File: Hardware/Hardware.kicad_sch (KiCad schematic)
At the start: 0 parts

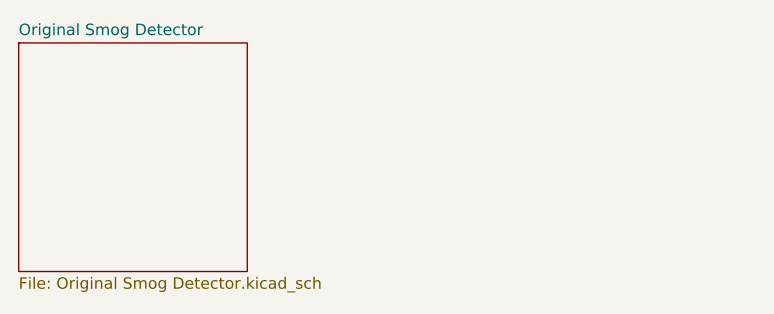
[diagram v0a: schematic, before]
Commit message: Made sheet Signal Amplification
will handle
- AC coupling of input
- DC biasing to 3V3/2
- Amplification by approx *-60
- Lowpass based anti-aliasing
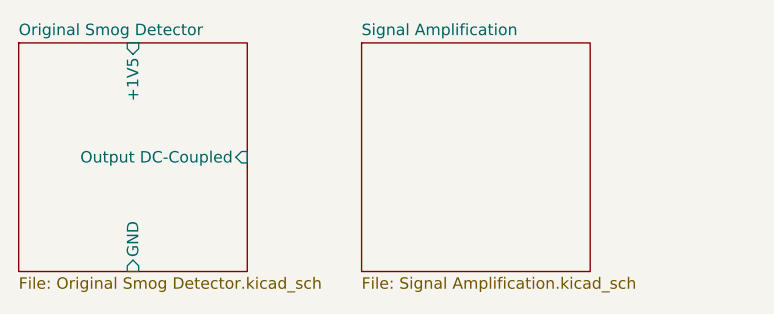
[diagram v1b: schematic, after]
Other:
- added sheet Signal Amplification (Signal Amplification.kicad_sch)
- sheet Original Smog Detector ports: added +1V5, GND, Output DC-Coupled; removed none
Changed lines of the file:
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@@
+			)
+		)
+		(pin "GND" input
+			(at 38.1 50.8 270)
+			(effects
+				(font
+					(size 1.27 1.27)
+				)
+				(justify left)
+			)
+		)
+		(pin "+1V5" input
+			(at 38.1 25.4 90)
+			(effects
+				(font
+					(size 1.27 1.27)
+				)
+				(justify right)
+			)
+		)
+		(pin "Output DC-Coupled" input
+			(at 50.8 38.1 0)
+			(effects
+				(font
+					(size 1.27 1.27)
+				)
+				(justify right)
 			)
 		)
@@
 				)
 			)
+		)
+	)
+	(sheet
+		(at 63.5 25.4)
+		(size 25.4 25.4)
+		(fields_autoplaced yes)
+		(stroke
+			(width 0.1524)
+			(type solid)
+		)
+		(fill
+			(color 0 0 0 0.0000)
+		)
+		(property "Sheetname" "Signal Amplification"
+			(at 63.5 24.6884 0)
+			(effects
+				(font
+					(size 1.27 1.27)
+				)
+				(justify left bottom)
+			)
+		)
+		(property "Sheetfile" "Signal Amplification.kicad_sch"
+			(at 63.5 51.3846 0)
+			(effects
+				(font
+					(size 1.27 1.27)
+				)
+				(justify left top)
+			)
+		)
+		(instances
+			(project "Hardware"
+				(path "/4e457c11-25d4-4677-9942-6ed7396aaf8a"
+					(page "3")
+				)
+			)

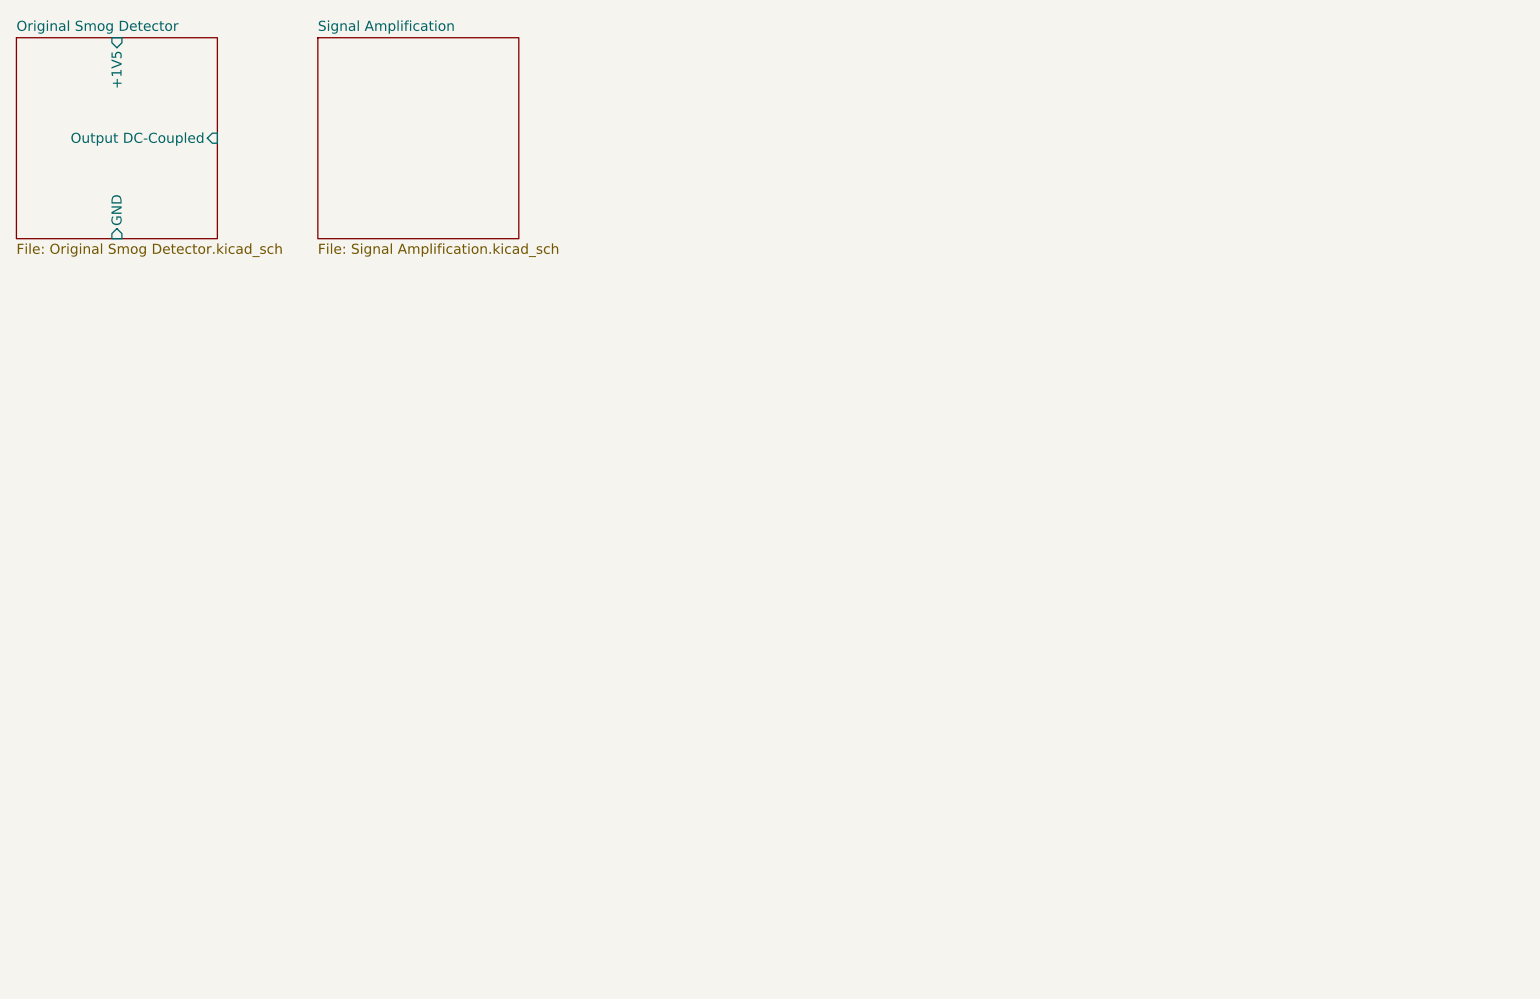
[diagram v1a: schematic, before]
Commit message: split some of the text and grouped the circuits better
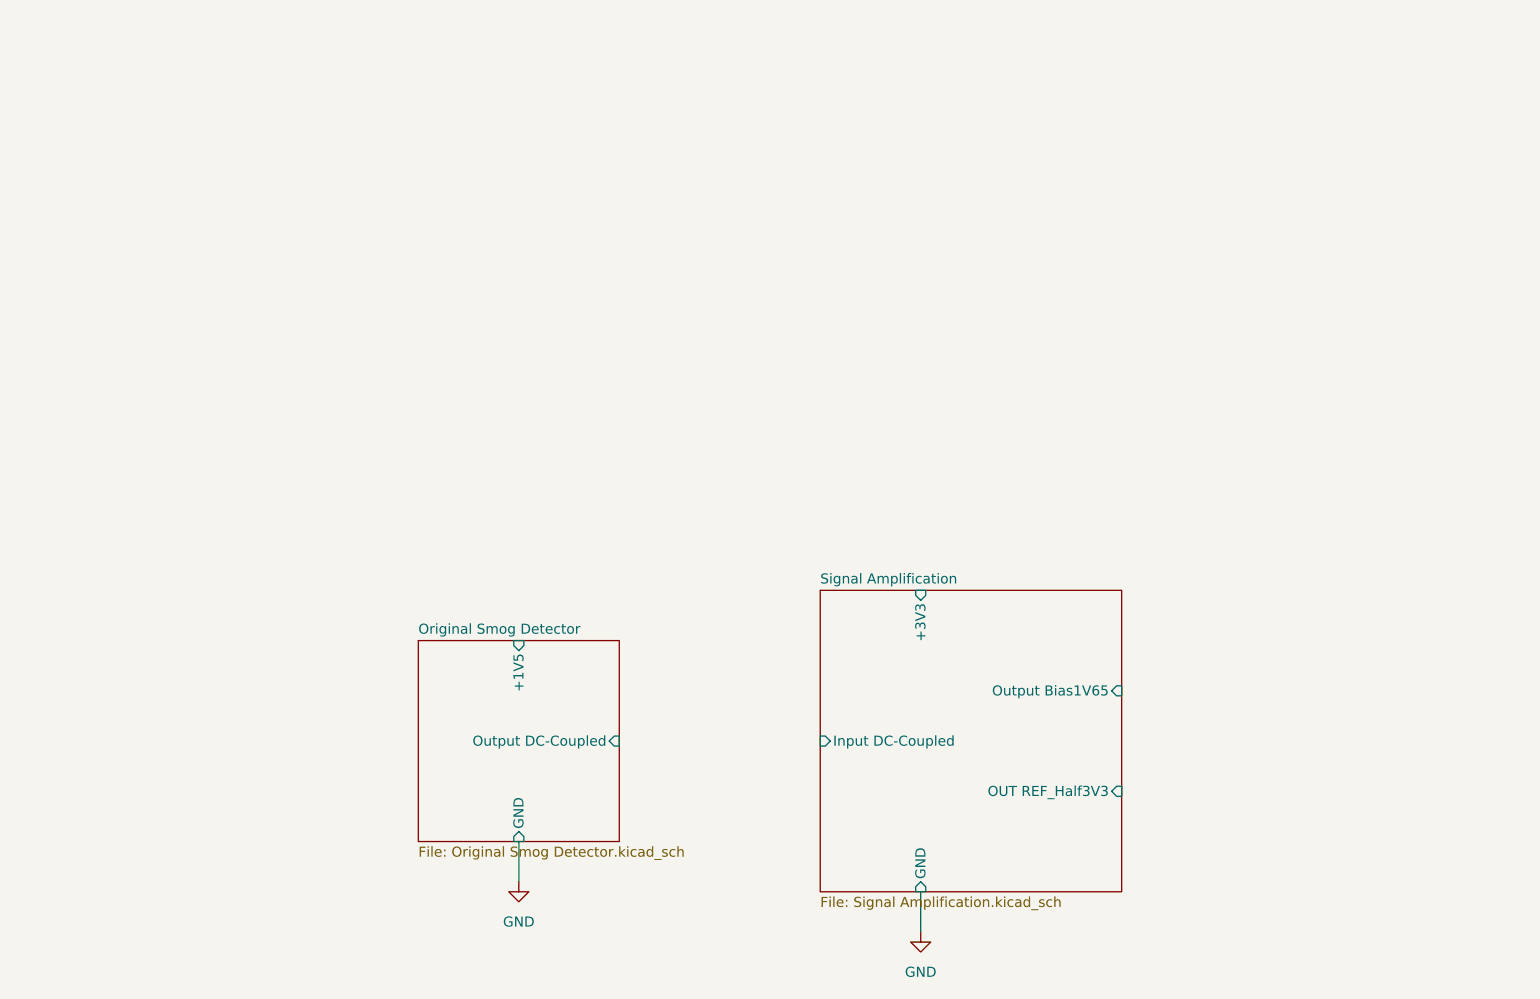
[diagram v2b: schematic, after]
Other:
- sheet Signal Amplification ports: added +3V3, GND, Input DC-Coupled, OUT REF_Half3V3, Output Bias1V65; removed none
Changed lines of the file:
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@@
 	(generator_version "8.0")
 	(paper "A4")
+	(wire
+		(pts
+			(xy 139.7 133.35) (xy 139.7 138.43)
+		)
+		(stroke
+			(width 0)
+			(type default)
+		)
+	)
+	(wire
+		(pts
+			(xy 88.9 127) (xy 88.9 132.08)
+		)
+		(stroke
+			(width 0)
+			(type default)
+		)
+	)
+	(symbol
+		(lib_id "power:GND")
+		(at 139.7 138.43 0)
+		(unit 1)
+		(exclude_from_sim no)
+		(in_bom yes)
+		(on_board yes)
+		(dnp no)
+		(fields_autoplaced yes)
+		(property "Reference" "#PWR02"
+			(at 139.7 144.78 0)
+			(effects
+				(font
+					(size 1.27 1.27)
+				)
+				(hide yes)
+			)
+		)
+		(property "Value" "GND"
+			(at 139.7 143.51 0)
+			(effects
+				(font
+					(size 1.27 1.27)
+				)
+			)
+		)
+		(property "Footprint" ""
+			(at 139.7 138.43 0)
+			(effects
+				(font
+					(size 1.27 1.27)
+				)
+				(hide yes)
+			)
+		)
+		(property "Datasheet" ""
+			(at 139.7 138.43 0)
+			(effects
+				(font
+					(size 1.27 1.27)
+				)
+				(hide yes)
+			)
+		)
+		(property "Description" "Power symbol creates a global label with name \"GND\" , ground"
+			(at 139.7 138.43 0)
+			(effects
+				(font
+					(size 1.27 1.27)
+				)
+				(hide yes)
+			)
+		)
+		(pin "1"
+		)
+		(instances
+			(project ""
+				(path "/4e457c11-25d4-4677-9942-6ed7396aaf8a"
+					(reference "#PWR02")
+					(unit 1)
+				)
+			)
+		)
+	)
+	(symbol
+		(lib_id "power:GND")
+		(at 88.9 132.08 0)
+		(unit 1)
+		(exclude_from_sim no)
+		(in_bom yes)
+		(on_board yes)
+		(dnp no)
+		(fields_autoplaced yes)
+		(property "Reference" "#PWR01"
+			(at 88.9 138.43 0)
+			(effects
+				(font
+					(size 1.27 1.27)
+				)
+				(hide yes)
+			)
+		)
+		(property "Value" "GND"
+			(at 88.9 137.16 0)
+			(effects
+				(font
+					(size 1.27 1.27)
+				)
+			)
+		)
+		(property "Footprint" ""
+			(at 88.9 132.08 0)
+			(effects
+				(font
+					(size 1.27 1.27)
+				)
+				(hide yes)
+			)
+		)
+		(property "Datasheet" ""
+			(at 88.9 132.08 0)
+			(effects
+				(font
+					(size 1.27 1.27)
+				)
+				(hide yes)
+			)
+		)
+		(property "Description" "Power symbol creates a global label with name \"GND\" , ground"
+			(at 88.9 132.08 0)
+			(effects
+				(font
+					(size 1.27 1.27)
+				)
+				(hide yes)
+			)
+		)
+		(pin "1"
+		)
+		(instances
+			(project ""
+				(path "/4e457c11-25d4-4677-9942-6ed7396aaf8a"
+					(reference "#PWR01")
+					(unit 1)
+				)
+			)
+		)
+	)
 	(sheet
-		(at 25.4 25.4)
+		(at 76.2 101.6)
 		(size 25.4 25.4)
 		(fields_autoplaced yes)
@@
 		)
 		(property "Sheetname" "Original Smog Detector"
-			(at 25.4 24.6884 0)
+			(at 76.2 100.8884 0)
 			(effects
 				(font
@@
 		)
 		(property "Sheetfile" "Original Smog Detector.kicad_sch"
-			(at 25.4 51.3846 0)
+			(at 76.2 127.5846 0)
 			(effects
 				(font
@@
 		)
 		(pin "GND" input
-			(at 38.1 50.8 270)
+			(at 88.9 127 270)
 			(effects
 				(font
@@
 		)
 		(pin "+1V5" input
-			(at 38.1 25.4 90)
+			(at 88.9 101.6 90)
 			(effects
 				(font
@@
 		)
 		(pin "Output DC-Coupled" input
-			(at 50.8 38.1 0)
+			(at 101.6 114.3 0)
 			(effects
 				(font
@@
 	)
 	(sheet
-		(at 63.5 25.4)
-		(size 25.4 25.4)
+		(at 127 95.25)
+		(size 38.1 38.1)
 		(fields_autoplaced yes)
 		(stroke
@@
 		)
 		(property "Sheetname" "Signal Amplification"
-			(at 63.5 24.6884 0)
+			(at 127 94.5384 0)
 			(effects
 				(font
@@
 		)
 		(property "Sheetfile" "Signal Amplification.kicad_sch"
-			(at 63.5 51.3846 0)
+			(at 127 133.9346 0)
 			(effects
 				(font
@@
 			)
 		)
+		(pin "OUT REF_Half3V3" input
+			(at 165.1 120.65 0)
+			(effects
+				(font
+					(size 1.27 1.27)
+				)
+				(justify right)
+			)
+		)
+		(pin "+3V3" input
+			(at 139.7 95.25 90)
+			(effects
+				(font
+					(size 1.27 1.27)
+				)
+				(justify right)
+			)
+		)
+		(pin "GND" input
+			(at 139.7 133.35 270)
+			(effects
+				(font
+					(size 1.27 1.27)
+				)
+				(justify left)
+			)
+		)
+		(pin "Input DC-Coupled" input
+			(at 127 114.3 180)
+			(effects
+				(font
+					(size 1.27 1.27)
+				)
+				(justify left)
+			)
+		)
+		(pin "Output Bias1V65" input
+			(at 165.1 107.95 0)
+			(effects
+				(font
+					(size 1.27 1.27)
+				)
+				(justify right)
+			)
+		)

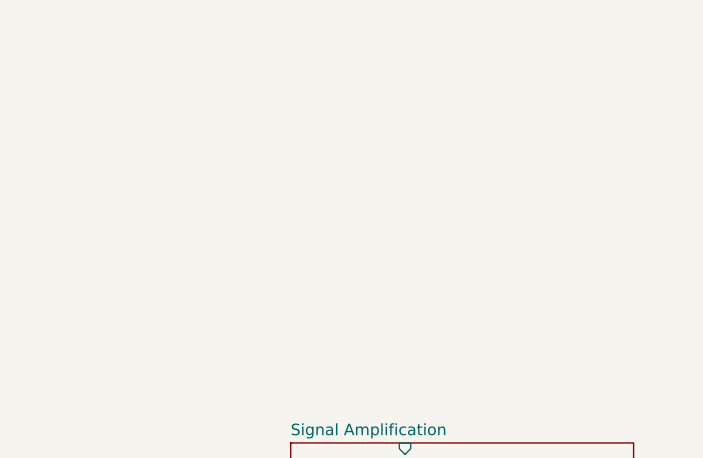
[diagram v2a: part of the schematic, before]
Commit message: made sheet PSU for power management
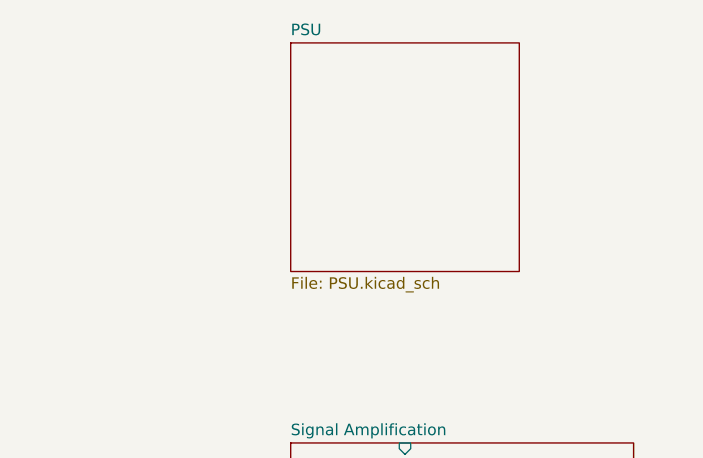
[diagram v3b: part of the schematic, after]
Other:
- added sheet PSU (PSU.kicad_sch)
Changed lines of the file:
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@@
+	)
+	(sheet
+		(at 127 50.8)
+		(size 25.4 25.4)
+		(fields_autoplaced yes)
+		(stroke
+			(width 0.1524)
+			(type solid)
+		)
+		(fill
+			(color 0 0 0 0.0000)
+		)
+		(property "Sheetname" "PSU"
+			(at 127 50.0884 0)
+			(effects
+				(font
+					(size 1.27 1.27)
+				)
+				(justify left bottom)
+			)
+		)
+		(property "Sheetfile" "PSU.kicad_sch"
+			(at 127 76.7846 0)
+			(effects
+				(font
+					(size 1.27 1.27)
+				)
+				(justify left top)
+			)
+		)
+		(instances
+			(project "Hardware"
+				(path "/4e457c11-25d4-4677-9942-6ed7396aaf8a"
+					(page "4")
+				)
+			)
+		)
 	)
 	(sheet

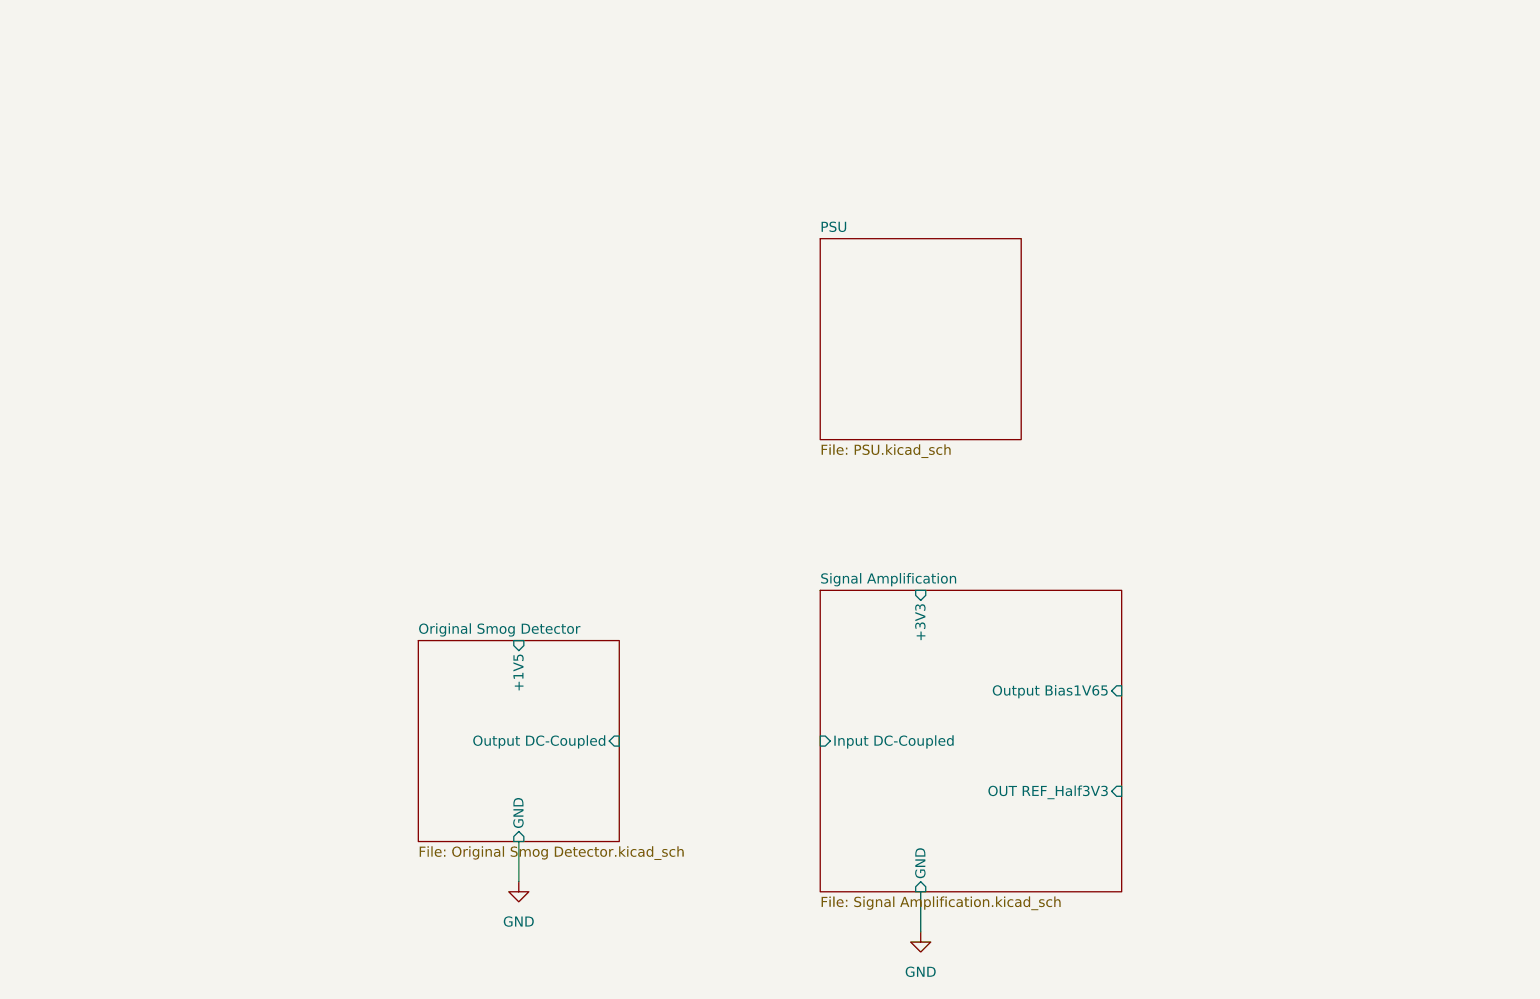
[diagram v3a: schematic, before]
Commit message: Did to much for one commit BAD
- calculated values for EN divider in PSU sheet
- added power flag to switch output in PSU sheet
- connected the different sheets in the Root page
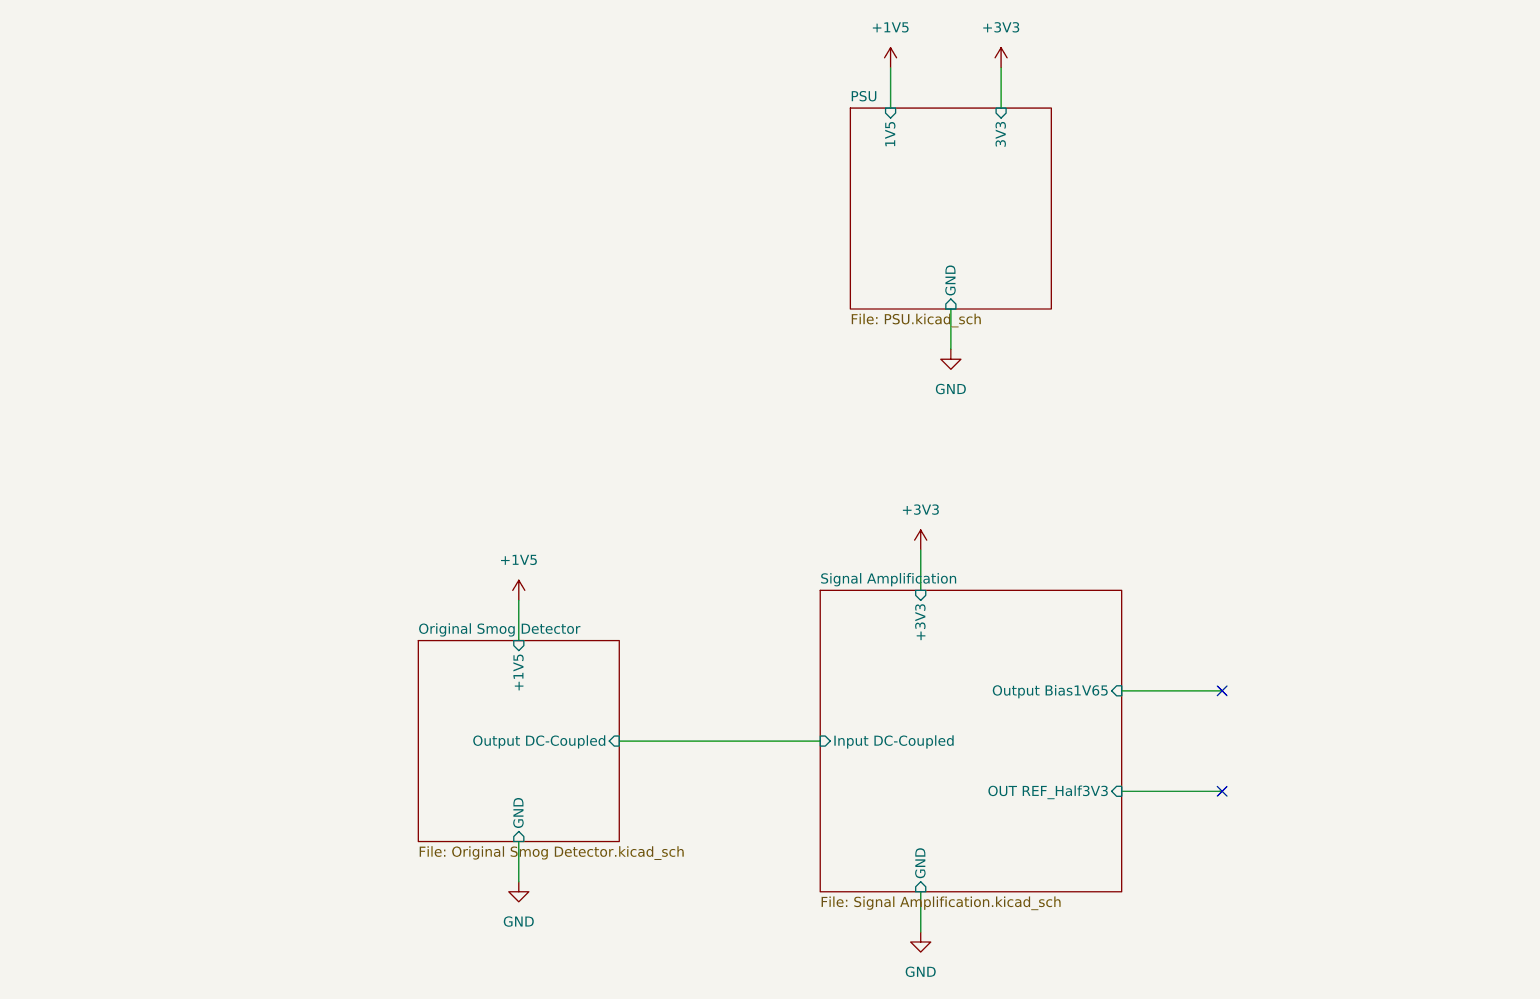
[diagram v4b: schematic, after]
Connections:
- no-connect marks 0 -> 2
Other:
- sheet PSU ports: added 1V5, 3V3, GND; removed none
